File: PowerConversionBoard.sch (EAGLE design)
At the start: 46 parts, among them U1 LM2678, U2 LM2678

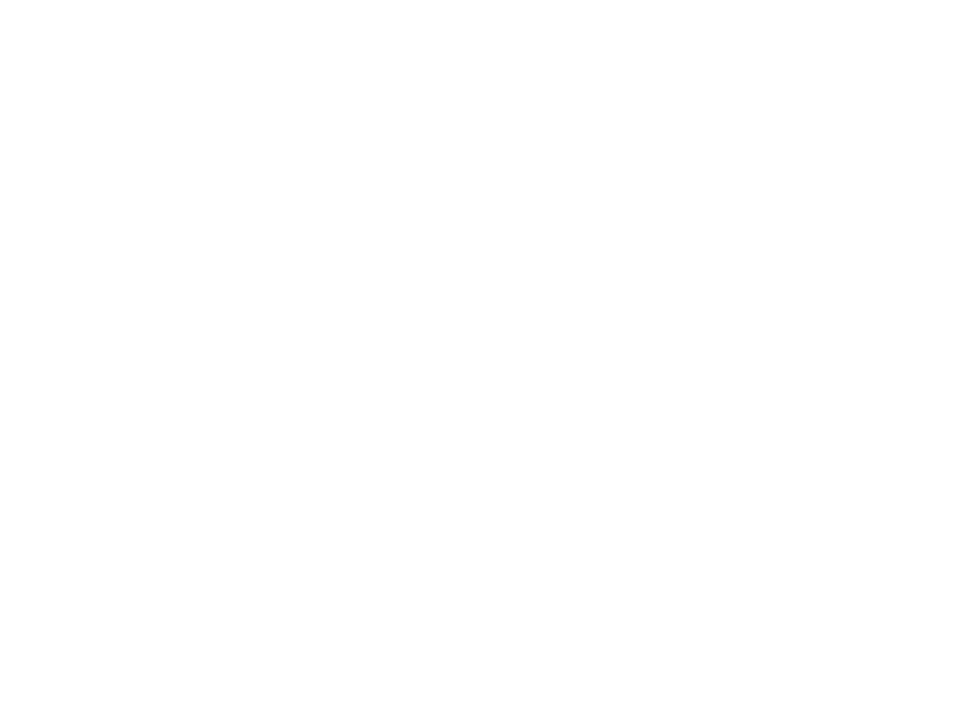
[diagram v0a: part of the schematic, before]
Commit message: added the power ditribution connector
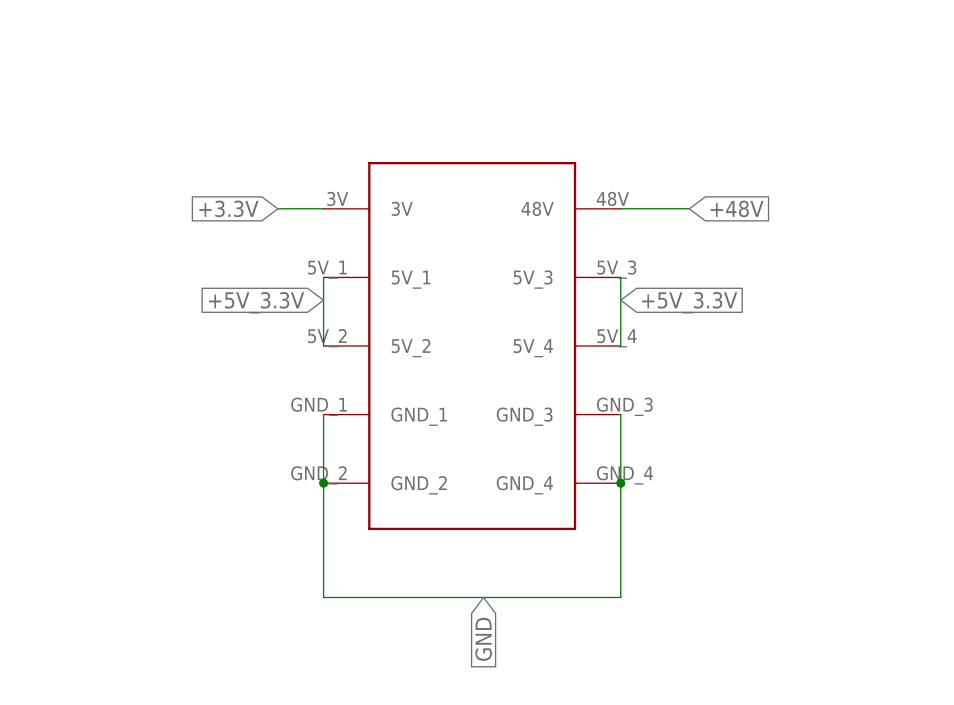
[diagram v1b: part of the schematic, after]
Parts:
- added U$4: DIST_TO_CONV, Dist_To_Conv_Connector:DIST_TO_CONV
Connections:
- net +3.3V: now also U$4.3V
- net +48V: now also U$4.48V
- net +5V_3.3V: now also U$4.5V_1, U$4.5V_2, U$4.5V_3, U$4.5V_4
- net GND: now also U$4.GND_1, U$4.GND_2, U$4.GND_3, U$4.GND_4
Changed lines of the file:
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@@
 <part name="5V_3.3_TP" library="TP" deviceset="TP" device=""/>
 <part name="U$6" library="5-33Regulator" deviceset="5-33REGULATOR" device=""/>
+<part name="U$4" library="Dist_To_Conv_Connector" deviceset="DIST_TO_CONV" device=""/>
 </parts>
 <sheets>
@@
 <attribute name="VALUE" x="355.6" y="-25.4" size="1.778" layer="96" rot="MR0"/>
 </instance>
+<instance part="U$4" gate="G$1" x="22.86" y="-215.9" smashed="yes"/>
 </instances>
 <busses>
@@
 <pinref part="D2" gate="G$1" pin="C"/>
 </segment>
+<segment>
+<pinref part="U$4" gate="G$1" pin="GND_3"/>
+<pinref part="U$4" gate="G$1" pin="GND_4"/>
+<wire x1="45.72" y1="-231.14" x2="45.72" y2="-238.76" width="0.1524" layer="91"/>
+<wire x1="45.72" y1="-238.76" x2="45.72" y2="-251.46" width="0.1524" layer="91"/>
+<wire x1="45.72" y1="-251.46" x2="12.7" y2="-251.46" width="0.1524" layer="91"/>
+<junction x="45.72" y="-238.76"/>
+<pinref part="U$4" gate="G$1" pin="GND_1"/>
+<pinref part="U$4" gate="G$1" pin="GND_2"/>
+<wire x1="12.7" y1="-231.14" x2="12.7" y2="-238.76" width="0.1524" layer="91"/>
+<wire x1="12.7" y1="-251.46" x2="12.7" y2="-238.76" width="0.1524" layer="91"/>
+<junction x="12.7" y="-238.76"/>
+<label x="30.48" y="-251.46" size="1.778" layer="95" rot="R270" xref="yes"/>
+</segment>
 </net>
 <net name="+5V" class="0">
@@
 <pinref part="+3.3" gate="G$1" pin="P$1"/>
 </segment>
+<segment>
+<pinref part="U$4" gate="G$1" pin="3V"/>
+<wire x1="12.7" y1="-208.28" x2="7.62" y2="-208.28" width="0.1524" layer="91"/>
+<label x="7.62" y="-208.28" size="1.778" layer="95" rot="R180" xref="yes"/>
+</segment>
 </net>
 <net name="N$2" class="0">
@@
 <wire x1="474.726" y1="-15.748" x2="467.106" y2="-15.748" width="0.1524" layer="91"/>
 <pinref part="5V_3.3_TP" gate="G$1" pin="P$1"/>
+</segment>
+<segment>
+<pinref part="U$4" gate="G$1" pin="5V_1"/>
+<pinref part="U$4" gate="G$1" pin="5V_2"/>
+<wire x1="12.7" y1="-215.9" x2="12.7" y2="-223.52" width="0.1524" layer="91"/>
+<label x="12.7" y="-218.44" size="1.778" layer="95" rot="R180" xref="yes"/>
+</segment>
+<segment>
+<pinref part="U$4" gate="G$1" pin="5V_3"/>
+<pinref part="U$4" gate="G$1" pin="5V_4"/>
+<wire x1="45.72" y1="-215.9" x2="45.72" y2="-223.52" width="0.1524" layer="91"/>
+<label x="45.72" y="-218.44" size="1.778" layer="95" xref="yes"/>
 </segment>
 </net>
@@
 <label x="362.55258125" y="81.480253125" size="1.778" layer="95" rot="R90" xref="yes"/>
 </segment>
-</net>
+<segment>
+<pinref part="U$4" gate="G$1" pin="48V"/>
+<wire x1="45.72" y1="-208.28" x2="53.34" y2="-208.28" width="0.1524" layer="91"/>
+<label x="53.34" y="-208.28" size="1.778" layer="95" xref="yes"/>
+</segment>
+</net>

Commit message: Align schematic to 0.1 in. Create board with dimension
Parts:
- U$2, U$7: value HCM1305 -> HCMA1305; device HCM1305:HCM1305 -> Inductor_15uH - hcma1305:HCMA1305
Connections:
- net +12V renamed N$11
- net +5V: no longer U1.FEEDBACK
- net N$1: now also U1.FEEDBACK
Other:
- moved on the sheet: +3.3, +3.3V, +5V, 5V, 5V_3.3, 5V_3.3_TP, C10, C11, C12, C14, C15, C16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

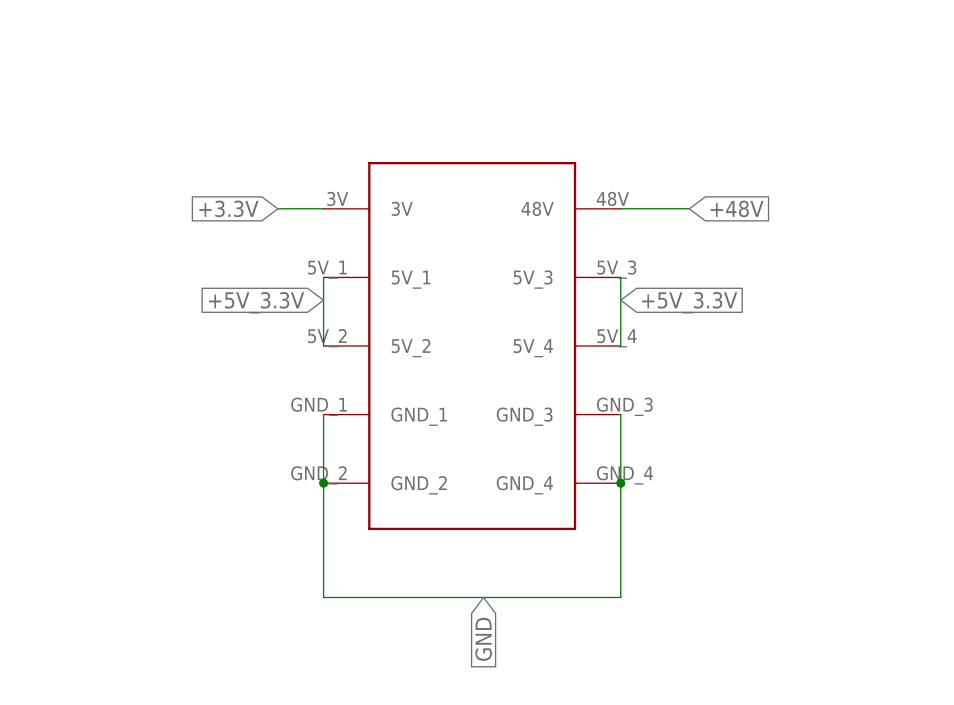
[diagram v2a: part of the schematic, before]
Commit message: Added the connector to the distribution board
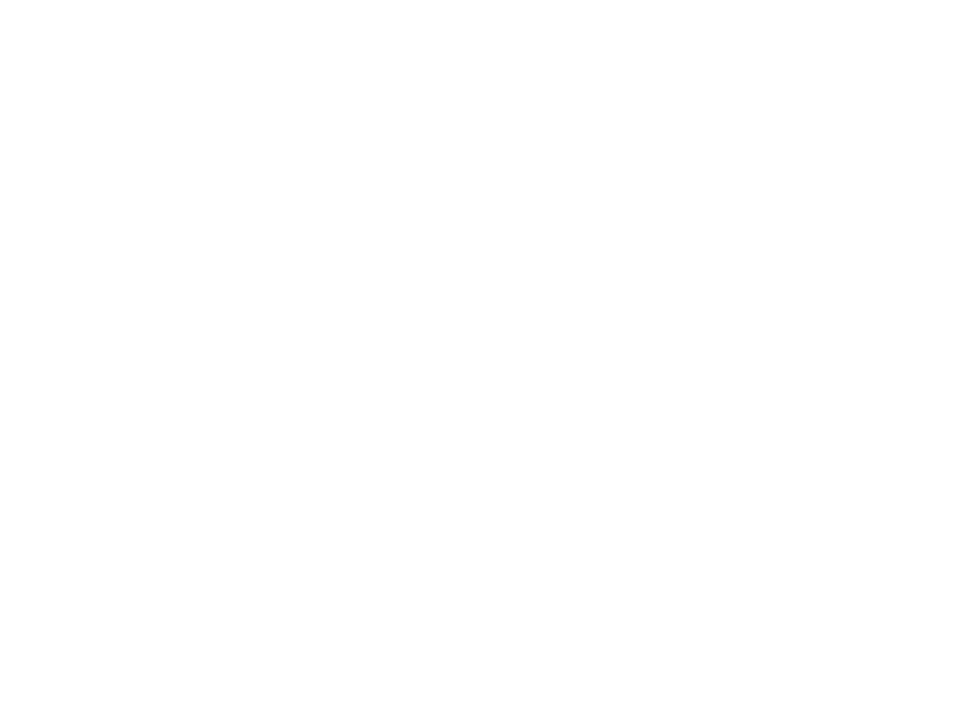
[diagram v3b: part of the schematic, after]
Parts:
- removed U$4: DIST_TO_CONV, Dist_To_Conv_Connector:DIST_TO_CONV
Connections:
- net +3.3V: no longer U$4.3V
- net +48V: no longer U$4.48V
- net +5V_3.3V: no longer U$4.5V_1, U$4.5V_2, U$4.5V_3, U$4.5V_4
- net GND: no longer U$4.GND_1, U$4.GND_2, U$4.GND_3, U$4.GND_4
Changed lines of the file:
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@@
 <part name="5V_3.3_TP" library="TP" deviceset="TP" device=""/>
 <part name="U$6" library="5-33Regulator" deviceset="5-33REGULATOR" device=""/>
-<part name="U$4" library="Dist_To_Conv_Connector" deviceset="DIST_TO_CONV" device=""/>
 </parts>
 <sheets>
@@
 <attribute name="VALUE" x="509.27" y="87.63" size="1.778" layer="96" rot="MR0"/>
 </instance>
-<instance part="U$4" gate="G$1" x="175.26" y="-101.6" smashed="yes"/>
 </instances>
 <busses>
@@
 <wire x1="38.1" y1="177.8" x2="38.1" y2="170.18" width="0.1524" layer="91"/>
 <pinref part="D2" gate="G$1" pin="C"/>
-</segment>
-<segment>
-<pinref part="U$4" gate="G$1" pin="GND_3"/>
-<pinref part="U$4" gate="G$1" pin="GND_4"/>
-<wire x1="198.12" y1="-116.84" x2="198.12" y2="-124.46" width="0.1524" layer="91"/>
-<wire x1="198.12" y1="-124.46" x2="198.12" y2="-137.16" width="0.1524" layer="91"/>
-<wire x1="198.12" y1="-137.16" x2="165.1" y2="-137.16" width="0.1524" layer="91"/>
-<junction x="198.12" y="-124.46"/>
-<pinref part="U$4" gate="G$1" pin="GND_1"/>
-<pinref part="U$4" gate="G$1" pin="GND_2"/>
-<wire x1="165.1" y1="-116.84" x2="165.1" y2="-124.46" width="0.1524" layer="91"/>
-<wire x1="165.1" y1="-137.16" x2="165.1" y2="-124.46" width="0.1524" layer="91"/>
-<junction x="165.1" y="-124.46"/>
-<label x="182.88" y="-137.16" size="1.778" layer="95" rot="R270" xref="yes"/>
 </segment>
 <segment>
@@
 <pinref part="+3.3" gate="G$1" pin="P$1"/>
 </segment>
-<segment>
-<pinref part="U$4" gate="G$1" pin="3V"/>
-<wire x1="165.1" y1="-93.98" x2="160.02" y2="-93.98" width="0.1524" layer="91"/>
-<label x="160.02" y="-93.98" size="1.778" layer="95" rot="R180" xref="yes"/>
-</segment>
 </net>
 <net name="N$2" class="0">
@@
 <wire x1="627.38" y1="96.52" x2="619.76" y2="96.52" width="0.1524" layer="91"/>
 <pinref part="5V_3.3_TP" gate="G$1" pin="P$1"/>
-</segment>
-<segment>
-<pinref part="U$4" gate="G$1" pin="5V_1"/>
-<pinref part="U$4" gate="G$1" pin="5V_2"/>
-<wire x1="165.1" y1="-101.6" x2="165.1" y2="-109.22" width="0.1524" layer="91"/>
-<label x="165.1" y="-104.14" size="1.778" layer="95" rot="R180" xref="yes"/>
-</segment>
-<segment>
-<pinref part="U$4" gate="G$1" pin="5V_3"/>
-<pinref part="U$4" gate="G$1" pin="5V_4"/>
-<wire x1="198.12" y1="-101.6" x2="198.12" y2="-109.22" width="0.1524" layer="91"/>
-<label x="198.12" y="-104.14" size="1.778" layer="95" xref="yes"/>
 </segment>
 </net>
@@
 <label x="513.17458125" y="198.320253125" size="1.778" layer="95" rot="R90" xref="yes"/>
 </segment>
-<segment>
-<pinref part="U$4" gate="G$1" pin="48V"/>
-<wire x1="198.12" y1="-93.98" x2="205.74" y2="-93.98" width="0.1524" layer="91"/>
-<label x="205.74" y="-93.98" size="1.778" layer="95" xref="yes"/>
-</segment>
-</net>
+</net>

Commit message: made progress on the buck controller supporting circuitry
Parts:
- removed +12V, 5V, GND_TP: TP, TP:TP
- removed +5V, 12V, GND: (no value), SparkFun-Connectors:BANANA_CONN
- removed C10, C11, C12, C24, C25, C26: 150uF, PowerComponents:C-TANTALUM(10UF_150UF)
- removed C14, C15, C16, C17, C18, C29, C30, C31: 10uF, PowerComponents:C-TANTALUM(10UF_150UF)
- removed C20, C6: 10nF, SparkFun-Capacitors:10NF-0603-50V-10%
- removed C3, C7: 0.47uF, rcl:C-EUC0603
- removed R4: 1.2 ohms, SparkFun-Resistors:RESISTOR0603
- removed U$13: 47 uF, Nordic_nRF:CAPACITOR_0603_N
- removed U$3: SWITCHMODE_SCHOTTKY, PowerComponents:SWITCHMODE_SCHOTTKY
- removed U$6: 5-33REGULATOR, 5-33Regulator:5-33REGULATOR
- removed U1, U2: LM2678, PowerComponents:LM2678
- added CADJ: 1000pF, Nordic_nRF:CAPACITOR_0603_L
- added CBYP: 1uF, Nordic_nRF:CAPACITOR_0603_L
- added CIN: 3.17uF, Nordic_nRF:CAPACITOR_0603_L
- added CVCC: 0.47uF, Nordic_nRF:CAPACITOR_0603_L
- added J1, J2: (no value), SparkFun-Connectors:CONN_05
- added Q1: 4.3A/20V/54mΩ, SparkFun-DiscreteSemi:MOSFET_PCH-IRLML2244
- added R10, R11, R12, R13, R14, R9: (no value), SparkFun-Resistors:RESISTOR0603
- added R6: 3.3k, SparkFun-Resistors:3.3KOHM-0603-1/10W-1%
- added RADJ: 1875, SparkFun-Resistors:RESISTOR0603
- added RSEN: 0.01, SparkFun-Resistors:RESISTOR0603
- added RT: 7.77k, SparkFun-Resistors:RESISTOR0603
- added U$4: LM5085, Buck_Controller:LM5085
- added U$8: (no value), Nordic_nRF:CAPACITOR_0603_L
- added U3: AZ1117EH-3.3TRG1, Linear Regulator - AZ1117EH-3.3TRG1:AZ1117EH-3.3TRG1
- D1: value (none) -> 3A/40V/500mV; device SparkFun-LED:LED0603 -> SparkFun-DiscreteSemi:DIODE-SCHOTTKY-B340A
- R2: value 470 -> 10k; device SparkFun-Resistors:470OHM-0603-1/10W-1% -> SparkFun-Resistors:10KOHM-0603-1/10W-1%
- R5: value 470 -> 5k
- U$1: value SWITCHMODE_SCHOTTKY -> (none); device PowerComponents:SWITCHMODE_SCHOTTKY -> Nordic_nRF:INDUCTOR_0603_M
- U$2, U$7: value HCMA1305 -> (none); device Inductor_15uH - hcma1305:HCMA1305 -> Nordic_nRF:CAPACITOR_0603_L
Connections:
- removed net +5V: +5V.1, 5V.P$1, C10.+, C11.+, C12.+, R2.2, U$2.2
- removed net N$11: C15.+, C16.+, C17.+, C18.+, C7.1, U1.VIN
- removed net N$14: C6.1, U1.BOOST
- new net FB: R12.1, R13.2, U$4.FB, U$7.2
- new net ISEN: Q1.S, RSEN.2, U$4.ISEN
- new net N$3: CVCC.1, U$4.VCC
- new net N$9: R14.2, U$7.1, U$8.2
- new net PGATE: Q1.G, U$4.PGATE
- net +3.3V: now also J2.5, U3.OUT; no longer U$13.1, U$6.VOUT, U$6.VO_S
- net +48V: now also CBYP.1, CIN.1, CVCC.2, J1.5, RT.1, U$4.VIN; no longer +12V.P$1, 12V.1, C14.+, C29.+, C3.1, C30.+, C31.+, U2.VIN
- net +5V_3.3V: now also J2.1, J2.2, J2.3, J2.4, U3.IN; no longer C24.+, C25.+, C26.+, U$6.EN, U$6.VCC, U$7.2, U2.FEEDBACK
- net GND: now also CBYP.2, CIN.2, D1.A, J1.1, J1.2, J1.3, J1.4, R12.2, U$4.GND, U3.ADJ/GND; no longer C10.-, C11.-, C12.-, C14.-, C15.-, C16.-, C17.-, C18.-, C24.-, C25.-, C26.-, C29.-, C3.2, C30.-, C31.-, C7.2, D1.C, GND.1, GND_TP.P$1, R4.1, U$1.P$1, U$1.P$3, U$3.P$1, U$3.P$3, U$6.GND, U1.GND, U1.TABGND, U2.GND, U2.TABGND
- net N$1: now also CADJ.1, RADJ.1, U$4.ADJ; no longer C6.2, U$1.P$4, U$2.1, U1.FEEDBACK, U1.OUTPUT
- net N$10: now also R13.1, U$1.2, U$8.1; no longer R4.2, U$13.2
- net N$2: now also CADJ.2, RADJ.2, RSEN.1; no longer C20.1, U2.BOOST
- net N$7: now also D1.C, Q1.D, R14.1, U$1.1; no longer C20.2, U$3.P$4, U$7.1, U2.OUTPUT
- net N$8: now also RT.2, U$4.RT; no longer D1.A, R2.1
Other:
- moved on the sheet: +3.3, +3.3V, 5V_3.3, 5V_3.3_TP, D2, D3, D4, GND3, R1, R2, R3, R5

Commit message: threw the pieces onto the board in no particular order and finsihed the skeleton of the circuit around the buck controller. Still need to get the standard values for the inductors and capacitors, but finished the resistors. Also need to figure oit the MOSFET and Schottky diode
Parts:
- removed R10, R11, R12, R13, R14, R9: (no value), SparkFun-Resistors:RESISTOR0603
- removed R2: 10k, SparkFun-Resistors:10KOHM-0603-1/10W-1%
- removed R6: 3.3k, SparkFun-Resistors:3.3KOHM-0603-1/10W-1%
- removed U$2, U$7, U$8: (no value), Nordic_nRF:CAPACITOR_0603_L
- removed U$4: LM5085, Buck_Controller:LM5085
- added 3R: 470, SparkFun-Resistors:470OHM-0603-1/10W-1%
- added C1: 3300pF, Nordic_nRF:CAPACITOR_0201_M
- added C2: 0.1uF, Nordic_nRF:CAPACITOR_0201_M
- added COUPLE: 1nF, SparkFun-Capacitors:1.0NF/1000PF-0603-50V-10%
- added COUT: 100uF, Nordic_nRF:CAPACITOR_0201_M
- added L1: 12.4uH, Nordic_nRF:INDUCTOR_0201_M
- added RFB1: 3.3k, SparkFun-Resistors:RESISTOR0603
- added RFB2: 10k, SparkFun-Resistors:RESISTOR0603
- CADJ, CBYP, CIN, CVCC: device Nordic_nRF:CAPACITOR_0603_L -> Nordic_nRF:CAPACITOR_0201_M
- Q1: value 4.3A/20V/54mΩ -> 6.5A/20V/35mΩ; device SparkFun-DiscreteSemi:MOSFET_PCH-IRLML2244 -> SparkFun-DiscreteSemi:MOSFET_PCH-NDS8434
- R3: value 470 -> 9.1k; device SparkFun-Resistors:470OHM-0603-1/10W-1% -> SparkFun-Resistors:RESISTOR0603
- RADJ: value 1875 -> 1.8k
- RT: value 7.77k -> 77.7k
- U$1: value (none) -> LM5085; device Nordic_nRF:INDUCTOR_0603_M -> Buck_Controller:LM5085
- renumbered R1 to 1R, R5 to 5R
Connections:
- removed net +5V_3.3V: 1R.2, 5V_3.3.1, 5V_3.3_TP.P$1, J2.1, J2.2, J2.3, J2.4, U3.IN
- removed net FB: R12.1, R13.2, U$4.FB, U$7.2
- removed net ISEN: Q1.S, RSEN.2, U$4.ISEN
- removed net N$1: CADJ.1, RADJ.1, U$4.ADJ
- removed net N$8 (its old number): RT.2, U$4.RT
- removed net PGATE: Q1.G, U$4.PGATE
- new net +5V: 1R.2, 5V_3.3.1, 5V_3.3_TP.P$1, C1.1, COUPLE.1, COUT.1, J2.1, J2.2, J2.3, J2.4, L1.2, RFB2.1, U3.IN
- new net N$11: C1.2, C2.1, R3.2
- new net N$14: C2.2, RFB1.1, RFB2.2, U$1.FB
- new net N$2: CADJ.1, RADJ.1, U$1.ADJ
- net +3.3V: now also 3R.2; no longer R3.2
- net +48V: now also CVCC.1, RT.2, U$1.RT, U$1.VIN; no longer CVCC.2, U$4.VIN
- net GND: now also COUPLE.2, COUT.2, RFB1.2, U$1.GND; no longer R12.2, U$4.GND
- net N$10: now also D1.C, L1.1, Q1.D, R3.1; no longer R13.1, U$1.2, U$8.1
- net N$3: now also CVCC.2, U$1.VCC; no longer CVCC.1, U$4.VCC
- net N$5: now also 3R.1; no longer R3.1
- net N$7: now also Q1.G, U$1.PGATE; no longer D1.C, Q1.D, R14.1, U$1.1
- net N$9: now also Q1.S, RSEN.2, U$1.ISEN; no longer R14.2, U$7.1, U$8.2
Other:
- note added: "Change the RT pin input to the correct thing, it's probably not the 48V input"
- moved on the sheet: CADJ, CBYP, CIN, CVCC, D1, Q1, R3, RADJ, RSEN, RT
